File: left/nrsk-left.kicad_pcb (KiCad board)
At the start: 2 copper layers, 187 x 120.3 mm, 125 parts, among them J1 PJ-320D, J2 USB-C, J3 OLED 128x32, SW1 Esc, SW10 1, SW11 2, SW12 3, SW13 4, SW14 5, SW15 6, SW16 16, SW17 Tab, SW18 Q, SW19 W, SW2 F1, SW20 E, SW21 R, SW22 T, SW23 23, SW24 Ctrl, SW25 A, SW26 S, SW27 D, SW28 F, SW29 G, SW3 F2, SW30 30, SW31 Shift, SW32 Z, SW33 X, SW34 C, SW35 V, SW36 B, SW37 37, SW38 Ctrl, SW39 Opt, SW4 F3, SW40 Cmd, SW41 Space, SW42 Space, SW43 Space, SW44 44, SW5 F4, SW6 F5, SW7 F6, SW8 8, SW9 `, U1 ATmega32U4-AU, U2 USBLC6-2SC6, U3 AS5600-ASOM, Y1 16MHz

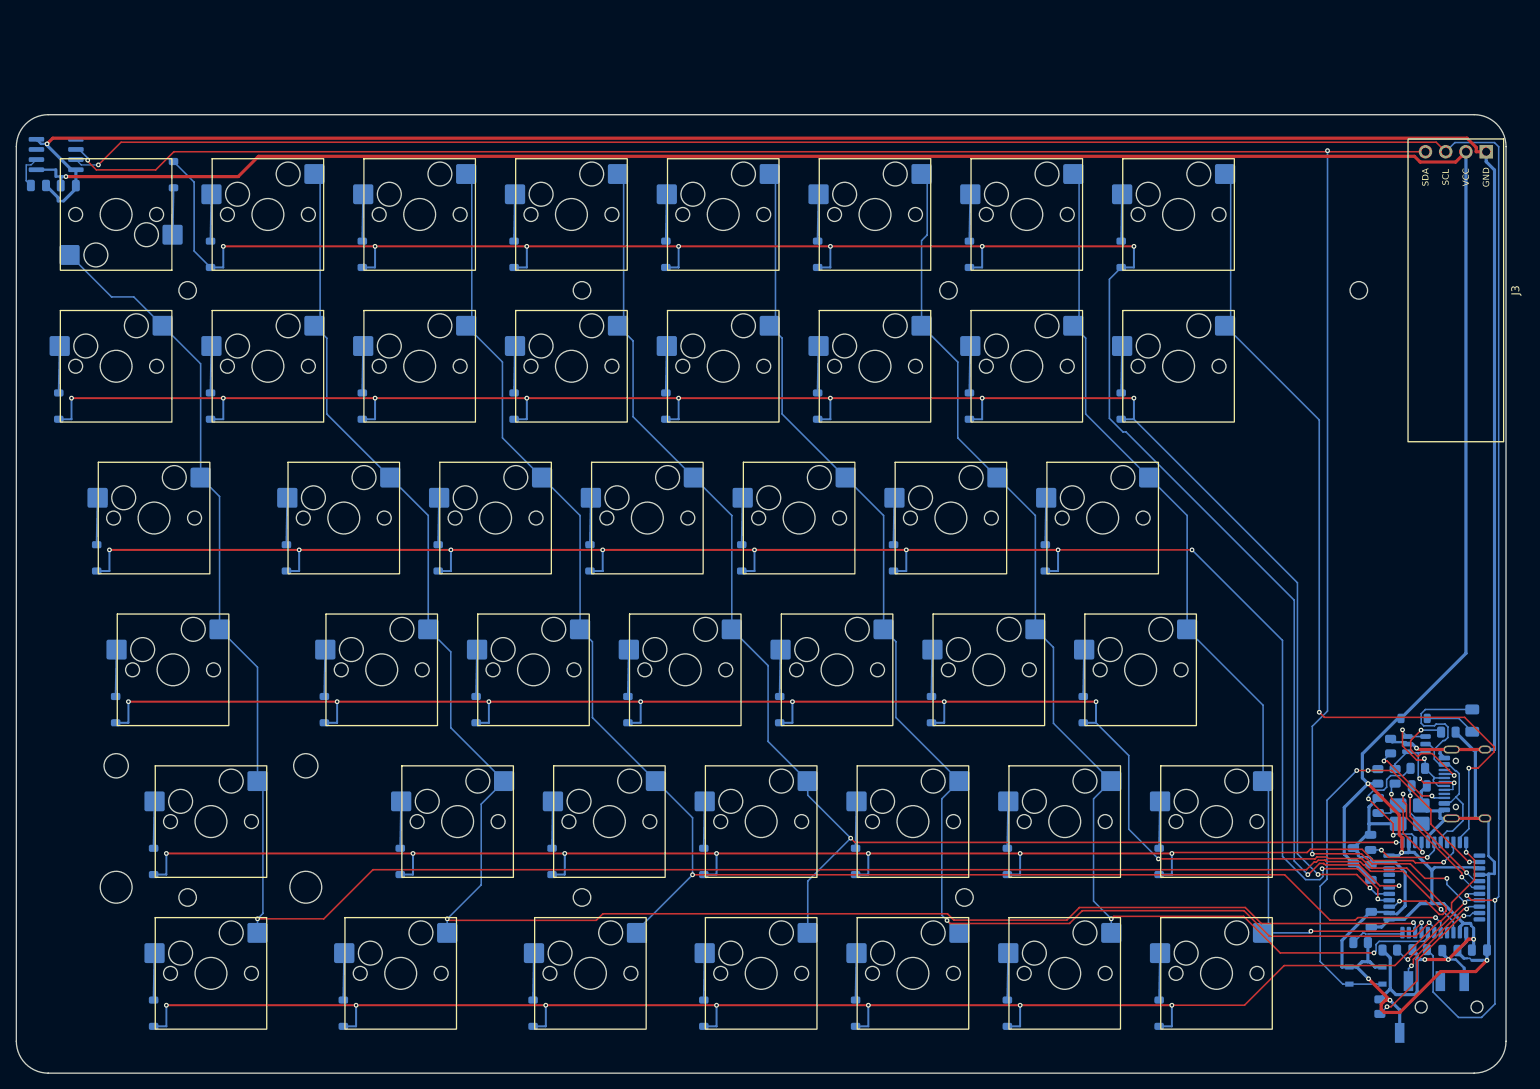
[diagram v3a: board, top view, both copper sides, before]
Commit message: Fit boards and cases tightly, align TRRS, add sourced BOM
- Board/case outlines shrink to each half's key area (left 163.2 mm,
  right 187.0 mm wide); TRRS jacks at the same height on both halves
- build.sh: per-step failure handling in the routing loop
- gen/doc_images.sh regenerates the README board/case images
- BOM: manufacturer part numbers, shops, prices and verified URLs
  from gen/bom_sources.json; README notes parts to check before ordering

Co-Authored-By: Claude Opus 5.5 <noreply@anthropic.com>
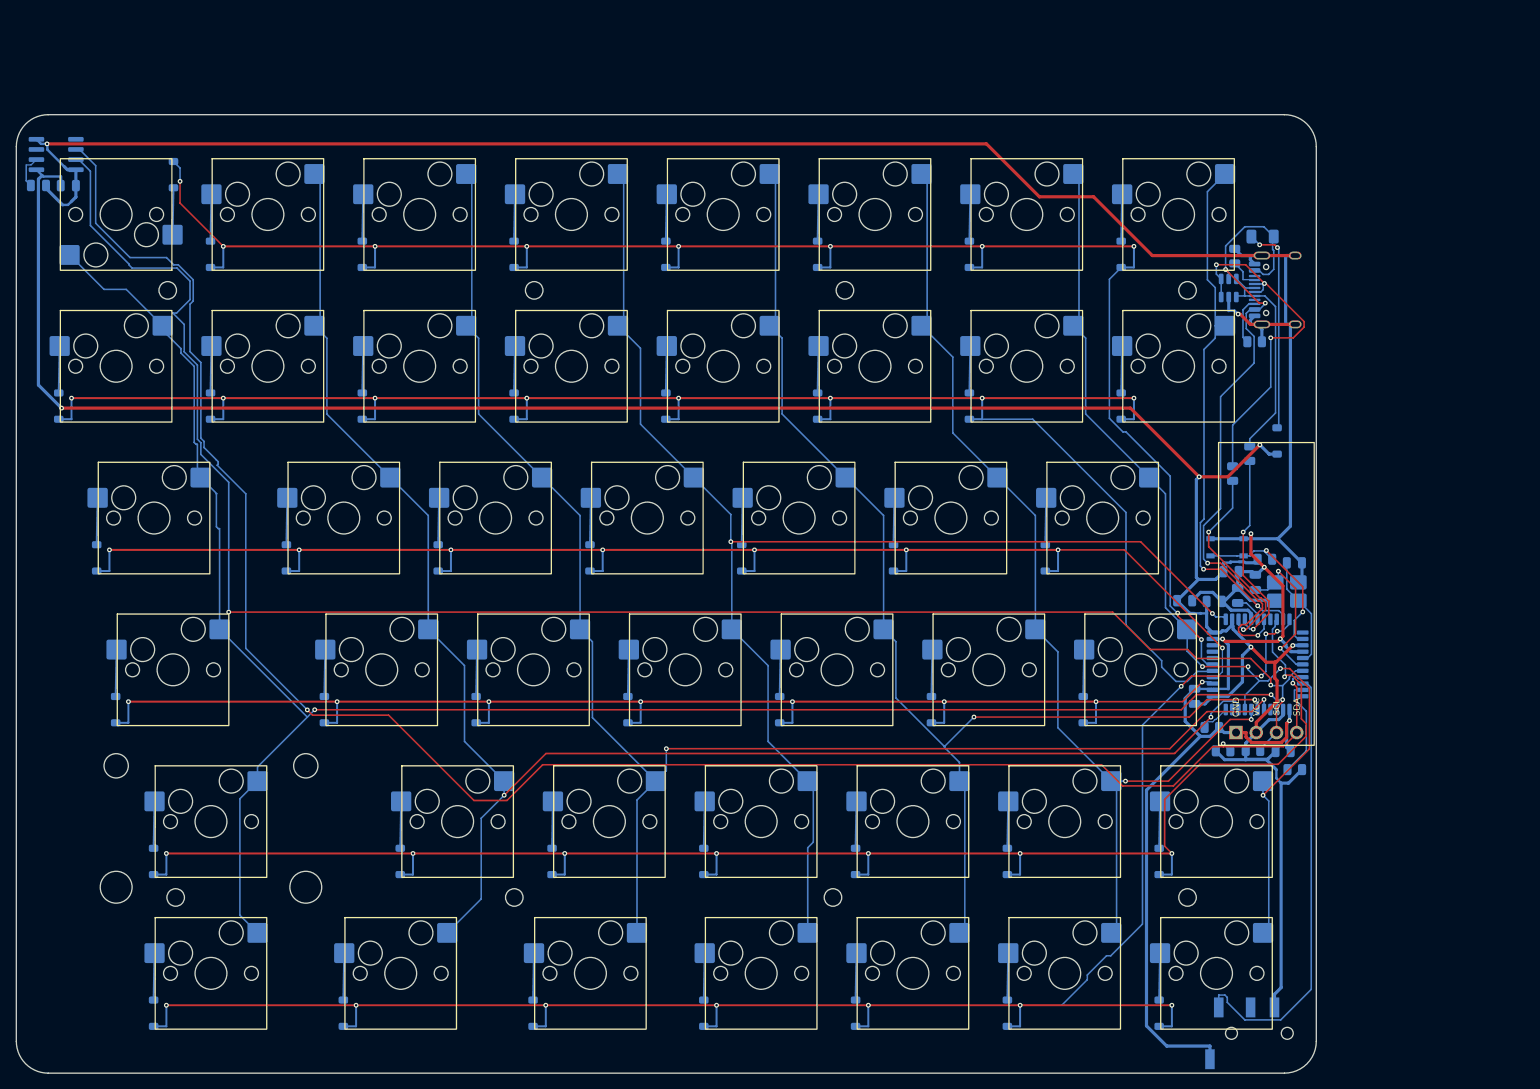
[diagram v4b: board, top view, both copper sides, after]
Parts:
- moved J2 66.4 mm to (186.5, 49.0)
- moved F1 66.2 mm to (183.4, 42.3), turned to 0 degrees
- moved R4 65.5 mm to (179.9, 44.8), turned to 90 degrees
- moved U2 61.9 mm to (179.2, 48.8), turned to 90 degrees
- moved C5 56.8 mm to (179.5, 84.3)
- moved RSW1 56.5 mm to (179.0, 81.3)
- moved R5 53.5 mm to (182.4, 55.5), turned to 0 degrees
- moved J3 44.9 mm to (183.9, 87.2), turned to 90 degrees
- moved R2 44.4 mm to (181.8, 69.5)
- moved R3 43.7 mm to (179.7, 72.0), turned to 90 degrees
- moved C4 39.3 mm to (177.3, 88.1), turned to 0 degrees
- moved D99 38.8 mm to (185.2, 68.0), turned to 90 degrees
- moved C7 38.4 mm to (173.6, 88.0), turned to 0 degrees
- moved C8 35.7 mm to (174.9, 100.0)
- moved U1 35.7 mm to (182.8, 96.0)
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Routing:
- net /SCL: track 309.9 -> 219.6 mm
- net /SDA: track 296.9 -> 230.7 mm, vias 6 -> 3
- net /ROW3: track 219.1 -> 166.9 mm, vias 9 -> 8
- net /VBUS: track 34.2 -> 82.2 mm, vias 0 -> 4
- net /ROW2: track 227.1 -> 179.1 mm, vias 10 -> 8
- net /ROW0: track 261.2 -> 213.7 mm, vias 9 -> 10
- net /COL7: track 111.2 -> 66.0 mm
- net VCC: track 362.9 -> 321.1 mm, vias 6 -> 5
- net /DATA: track 14.0 -> 55.6 mm, vias 2 -> 0
- net /RST: track 57.4 -> 23.0 mm, vias 3 -> 2
- net /USB_D-: track 15.2 -> 45.0 mm, vias 2 -> 3
- net GND: track 421.1 -> 393.2 mm, vias 5 -> 7
- net /COL1: track 233.6 -> 206.8 mm
- net /COL0: track 254.8 -> 228.0 mm
- net /ROW1: track 244.0 -> 219.2 mm, vias 10 -> 8
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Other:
- board size 187 x 120.3 mm -> 163.2 x 120.3 mm

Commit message: Align OLEDs, show KiCad-assembled boards in the viewer, add explode gap slider
- Left OLED moves to the top two rows like the right one; the left board
  grows 4.7 mm on the inner edge to keep the same switch clearance
- Footprints carry 3D models: kiswitch MX switch / Kailh socket /
  stabilizer, LCSC USB-C and PJ-320D (fetched by gen/fetch_3d.sh into
  tools/), and a simple OLED module model (gen/models3d.py)
- gen/export_3d.py exports each board as GLB; gen/glb_mesh.py merges,
  dedupes and quantises it into instanced meshes for case/preview/viewer.html
- Viewer: exploded view gets a layer-gap slider (0-40 mm)
- BOM/README: both LCSC TRRS jacks verified against the KiCad pad layout

Co-Authored-By: Claude Opus 5.5 <noreply@anthropic.com>
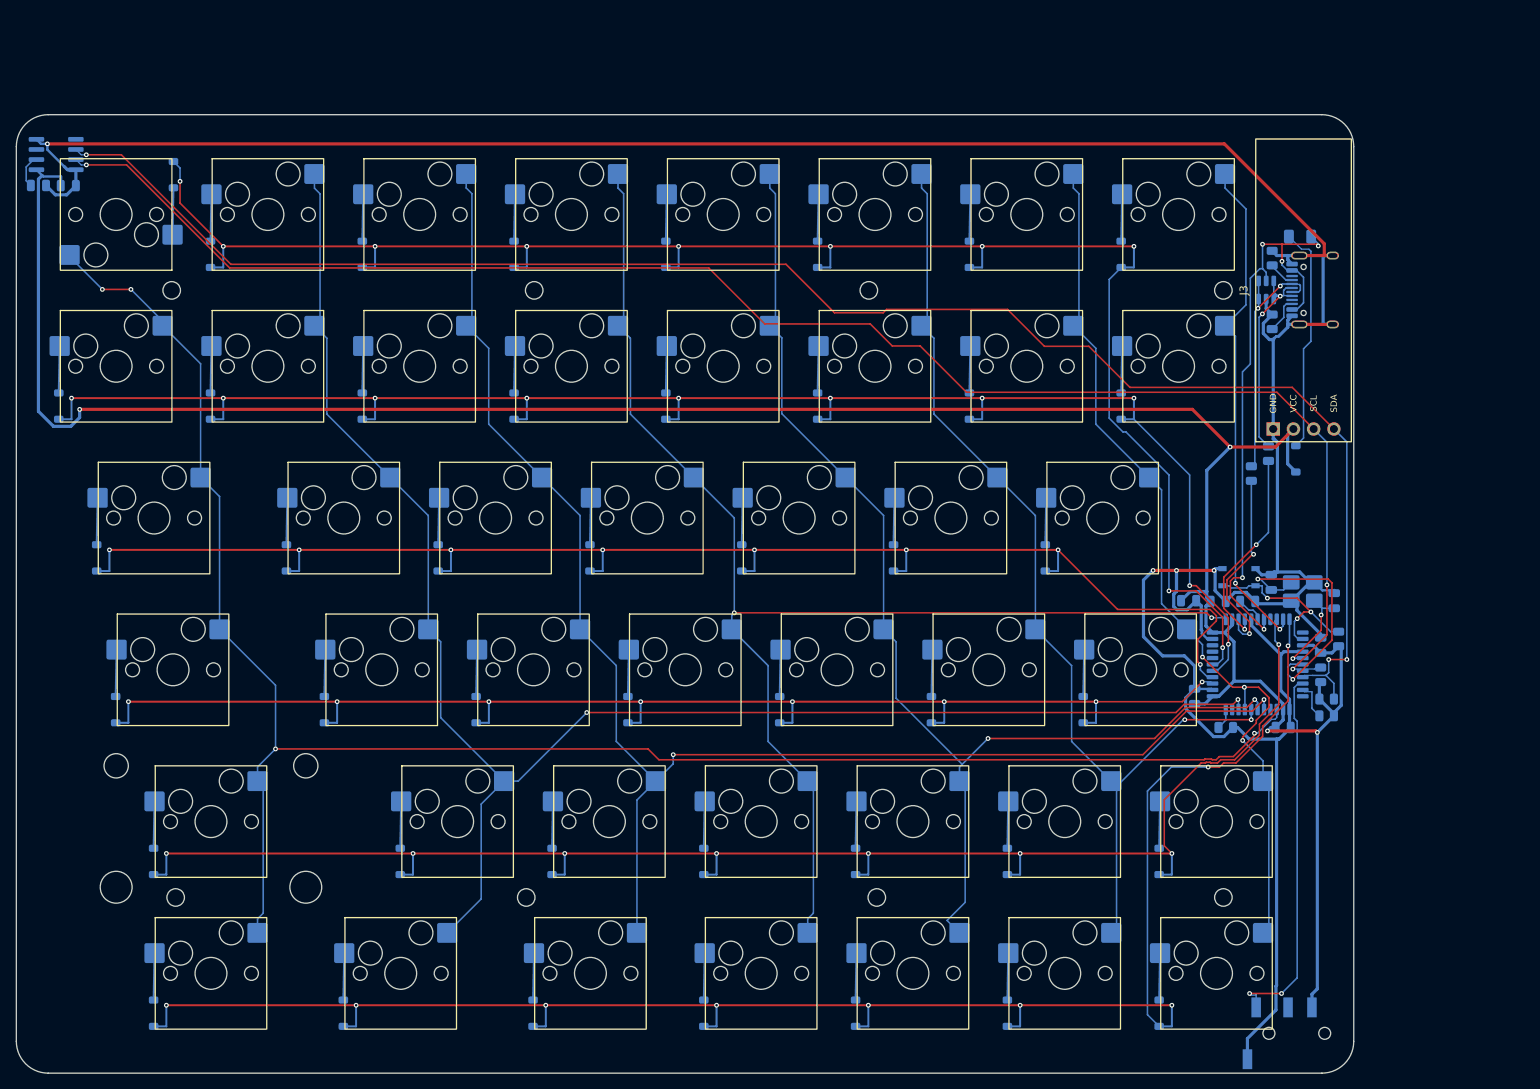
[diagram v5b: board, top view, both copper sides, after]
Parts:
- moved J3 38.4 mm to (188.6, 49.0)
- moved C5 14.6 mm to (190.7, 93.6), turned to 90 degrees
- moved R9 14.5 mm to (191.5, 100.3)
- moved R6 13.6 mm to (193.0, 92.8), turned to 90 degrees
- moved R8 12.7 mm to (190.7, 97.3), turned to 90 degrees
- moved R1 7.85 mm to (191.5, 102.5)
- moved C2 6.90 mm to (192.4, 88.0), turned to 90 degrees
- moved H7 5.50 mm to (135.0, 125.2)
- moved R4 4.71 mm to (184.6, 45.0)
- moved U2 4.71 mm to (183.9, 49.0)
- moved F1 4.70 mm to (188.1, 42.3)
- moved J1 4.70 mm to (186.4, 142.3)
- moved J2 4.70 mm to (191.2, 49.0)
- moved H4 4.50 mm to (178.5, 49.0)
- moved H8 4.50 mm to (178.5, 125.2)
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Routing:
- net /SDA: track 230.7 -> 213.2 mm
- net /SCL: track 219.6 -> 205.7 mm
- net /ROW1: track 219.2 -> 205.5 mm, vias 8 -> 10
- net GND: track 393.2 -> 406.3 mm, vias 7 -> 4
- net /XTAL1: track 19.6 -> 32.6 mm
- net /USB_D-: track 45.0 -> 32.0 mm, vias 3 -> 2
- net /COL6: track 125.0 -> 113.8 mm, vias 4 -> 3
- net /DATA: track 55.6 -> 47.1 mm, vias 0 -> 2
- net /ROW5: track 227.9 -> 219.5 mm, vias 11 -> 9
- net /HAND: track 12.6 -> 4.66 mm
- net /ROW4: track 201.7 -> 194.3 mm
- net /VBUS: track 82.2 -> 75.1 mm, vias 4 -> 5
- net /COL3: track 172.4 -> 168.6 mm
- net /ROW0: track 213.7 -> 216.7 mm
- net /ROW2: track 179.1 -> 181.9 mm
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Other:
- board size 163.2 x 120.3 mm -> 167.9 x 120.3 mm
